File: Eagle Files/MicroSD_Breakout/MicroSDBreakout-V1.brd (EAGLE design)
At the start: 33.1 x 22.9 mm, 2 parts

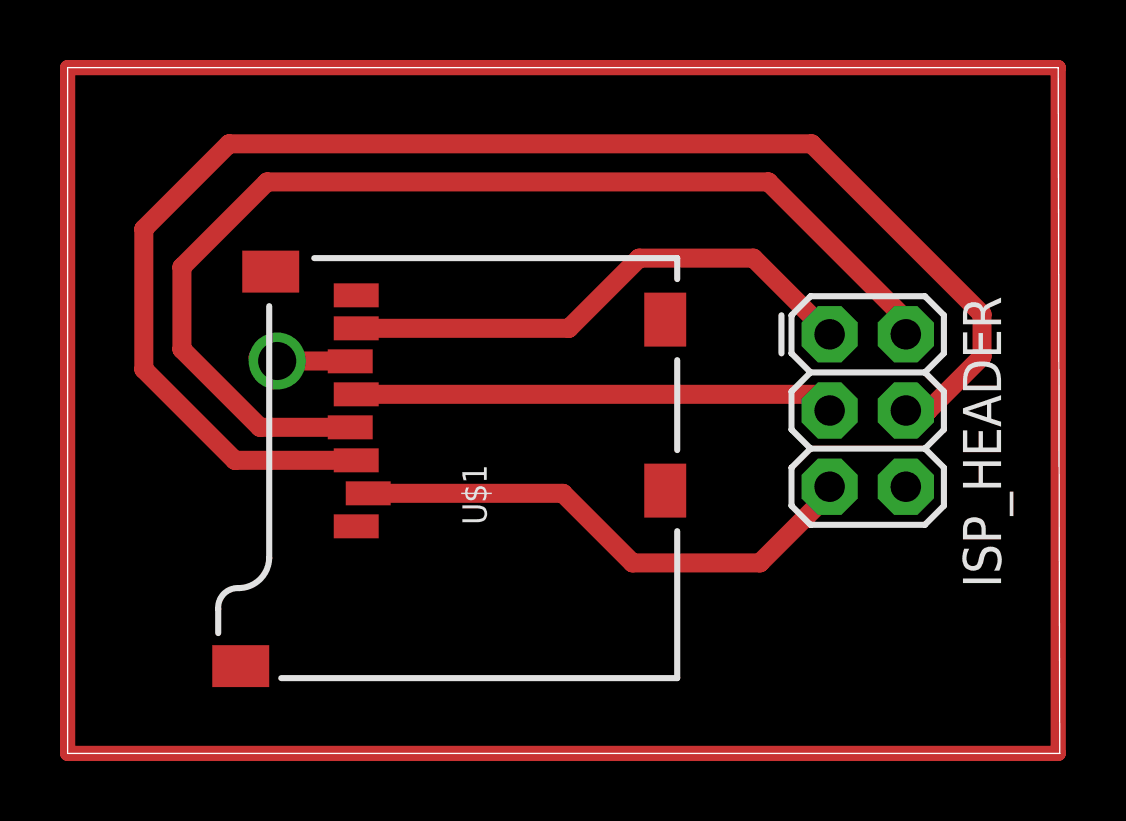
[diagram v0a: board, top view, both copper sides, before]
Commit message: MicroSD Breakout Board now has a pull up resistor on CS
--Arthur

git-svn-id: http://cd-net.net/CPE496/trunk@89 05b6d0e0-c345-4a8e-a5b7-579c8bd0b646
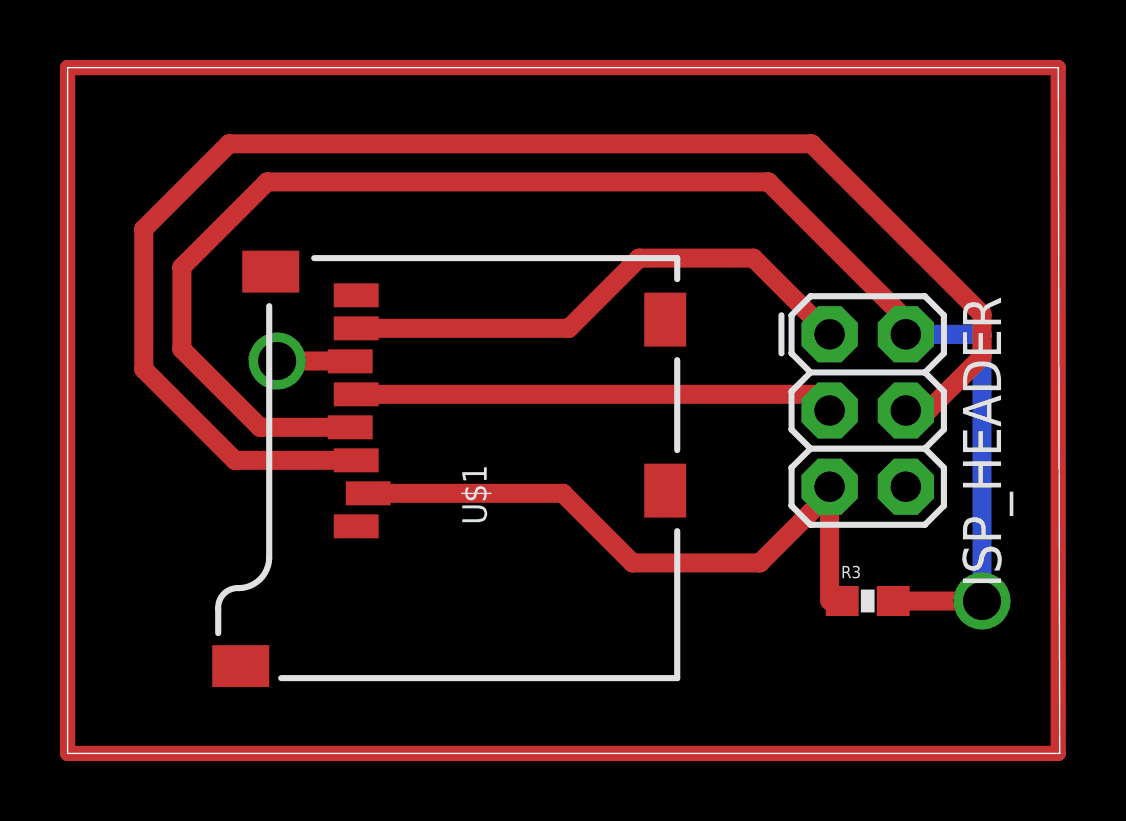
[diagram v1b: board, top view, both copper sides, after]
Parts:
- added R3: 10K, SparkFun:0603-RES
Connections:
- net 3.3V: now also R3.2
- net CS: now also R3.1
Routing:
- net 3.3V: track 37.1 -> 51.5 mm, vias 0 -> 1
- net CS: track 17.5 -> 21.8 mm

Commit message: Updated Boards
--Arthur

git-svn-id: http://cd-net.net/CPE496/trunk@93 05b6d0e0-c345-4a8e-a5b7-579c8bd0b646
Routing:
- net N$1: track 0.00 -> 111.8 mm
- net GND: track 4.12 -> 30.5 mm
- net 3.3V: track 51.5 -> 50.5 mm

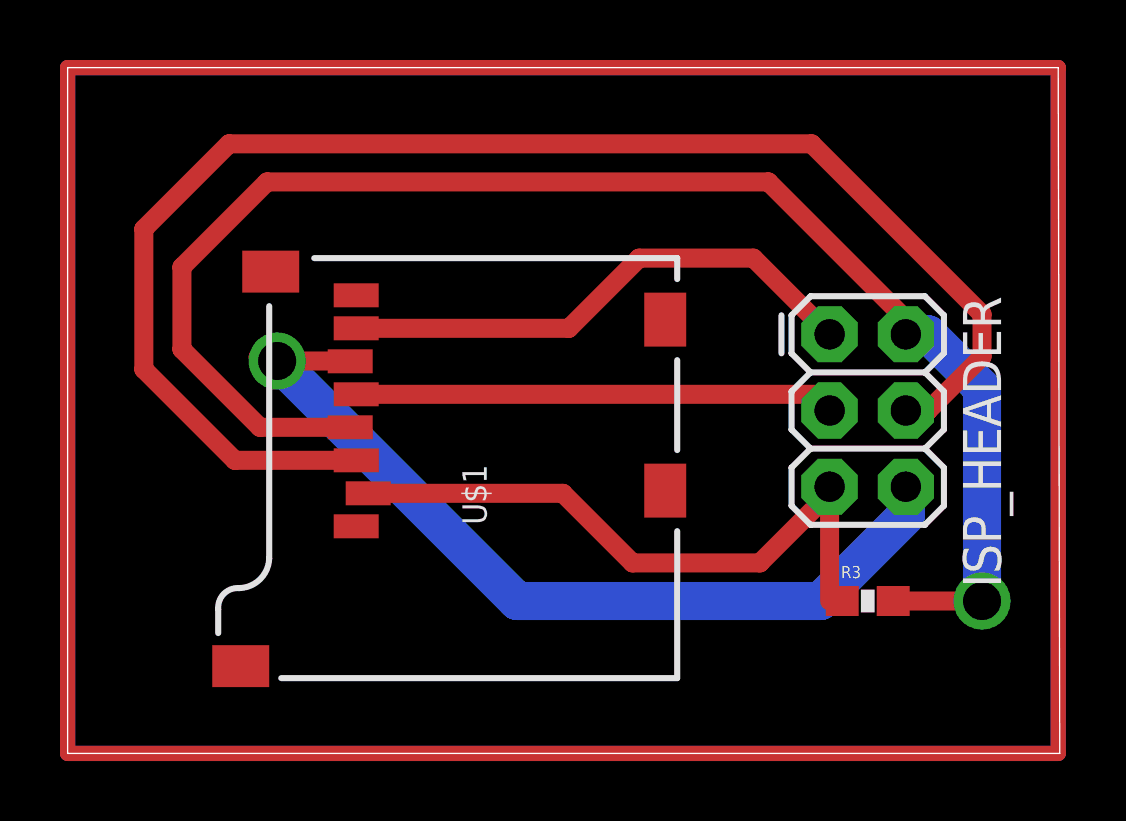
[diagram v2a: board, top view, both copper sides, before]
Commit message: Main Board with Headers is now almost ready.
I'm adding the FTDI Module right now.

TODO:
1.  Double check regulator Datasheet.  I think we're missing a capacitor.
2.  Update Radio Module Schematics to incorporate ground plane.
3.  Check if the hall effect sensor can work linearly at 3.3V
4.  Finish Adding FTDI chip and USB connector.

--Arthur

git-svn-id: http://cd-net.net/CPE496/trunk@119 05b6d0e0-c345-4a8e-a5b7-579c8bd0b646
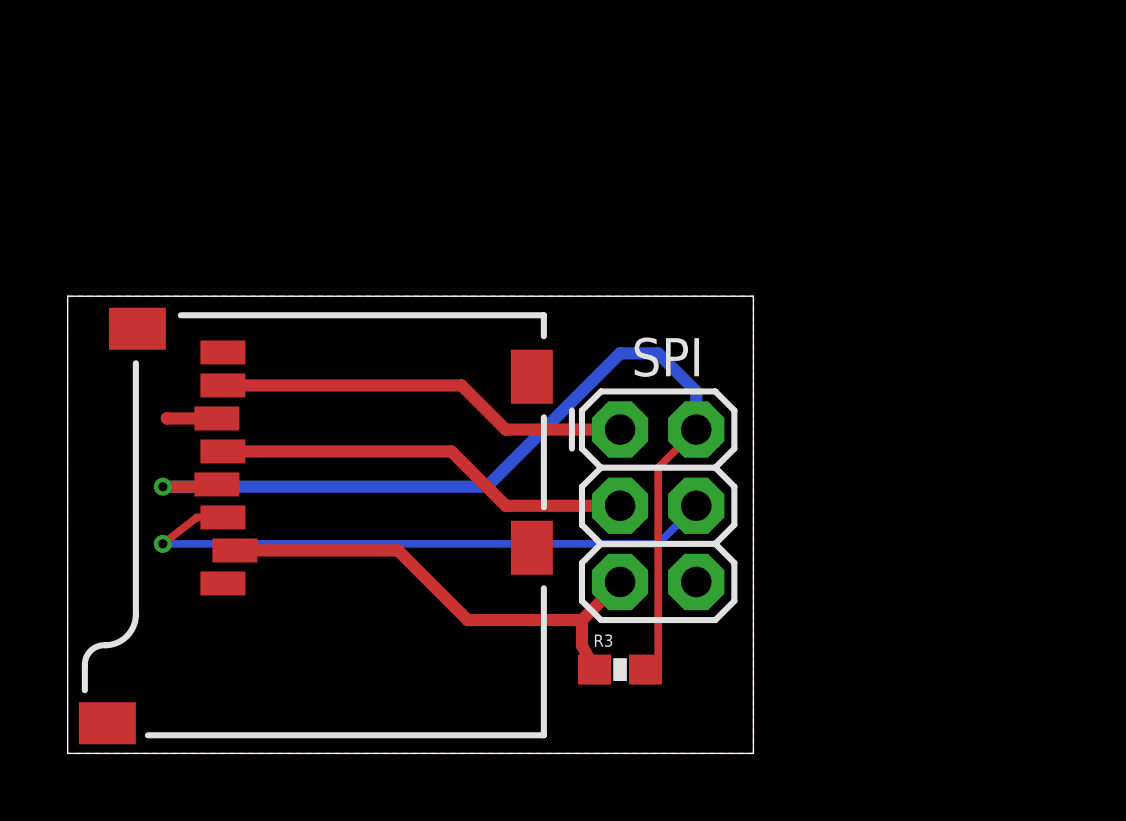
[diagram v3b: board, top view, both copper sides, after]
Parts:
- removed ISP_HEADER: AVR_SPI_PRG_6PTH, SparkFun:2X3
- added SPI: (no value), SparkFun:2X3
- moved R3 8.57 mm to (18.4, 2.79)
- moved U$1 4.84 mm to (15.9, 14.6)
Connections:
- net 3.3V: now also SPI.2; no longer ISP_HEADER.2
- net CS: now also SPI.5; no longer ISP_HEADER.5
- net GND: now also SPI.6; no longer ISP_HEADER.6
- net MISO: now also SPI.1; no longer ISP_HEADER.1
- net MOSI: now also SPI.4; no longer ISP_HEADER.4
- net SCK: now also SPI.3; no longer ISP_HEADER.3
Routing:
- net BORDER: track 111.8 -> 0.00 mm
- net N$1: track 111.8 -> 0.00 mm
- net GND: track 30.5 -> 1.68 mm, vias 1 -> 0
- net MOSI: track 49.2 -> 20.6 mm, vias 0 -> 1
- net 3.3V: track 50.5 -> 32.1 mm
- net CS: track 21.8 -> 16.1 mm
- net MISO: track 17.8 -> 13.8 mm
- net SCK: track 16.3 -> 14.0 mm
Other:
- board size 33.1 x 22.9 mm -> 22.9 x 15.2 mm
